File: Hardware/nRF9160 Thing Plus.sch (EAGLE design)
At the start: 89 parts, among them J1 USB Female C, J10 QWIIC_RIGHT_ANGLE, J2 CON-HEADER-1X12-MALE-PIN, J3 CON-HEADER-1X16-MALE-PIN, J4 CON-1909763-1, J6 CON-SIM-104224-0820, J7 CON-1909763-1, J8 CON-FTSH-105-XX-X-DV, Q1 MOSFET-P-SC89, Q2 MOSFET-DUAL-COMP-SOT563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

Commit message: Updated BOM
replaced SW1 and SW2 to new taller momentary switch
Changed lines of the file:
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@@
 <part name="GND11" library="supply1" library_urn="urn:adsk.eagle:library:371" deviceset="GND" device=""/>
 <part name="GND12" library="supply1" library_urn="urn:adsk.eagle:library:371" deviceset="GND" device=""/>
-<part name="SW1" library="SparkFun-Switches" deviceset="MOMENTARY-SWITCH-SPST" device="-SMD-4.6X2.8MM"/>
-<part name="SW2" library="SparkFun-Switches" deviceset="MOMENTARY-SWITCH-SPST" device="-SMD-4.6X2.8MM"/>
+<part name="SW1" library="SparkFun-Switches" deviceset="MOMENTARY-SWITCH-SPST" device="-SMD-4.6X2.8MM" value=""/>
+<part name="SW2" library="SparkFun-Switches" deviceset="MOMENTARY-SWITCH-SPST" device="-SMD-4.6X2.8MM" value=""/>
 <part name="GND13" library="supply1" library_urn="urn:adsk.eagle:library:371" deviceset="GND" device=""/>
 <part name="U6" library="nRF9160-IC" deviceset="FLASH" device="-WSON" package3d_urn="urn:adsk.eagle:package:19416409/2" override_package3d_urn="urn:adsk.eagle:package:19415944/2" override_package_urn="urn:adsk.eagle:footprint:19415945/1" override_locally_modified="yes" technology="-W25Q32JVZPIQ" value="FLASH-WSON"/>

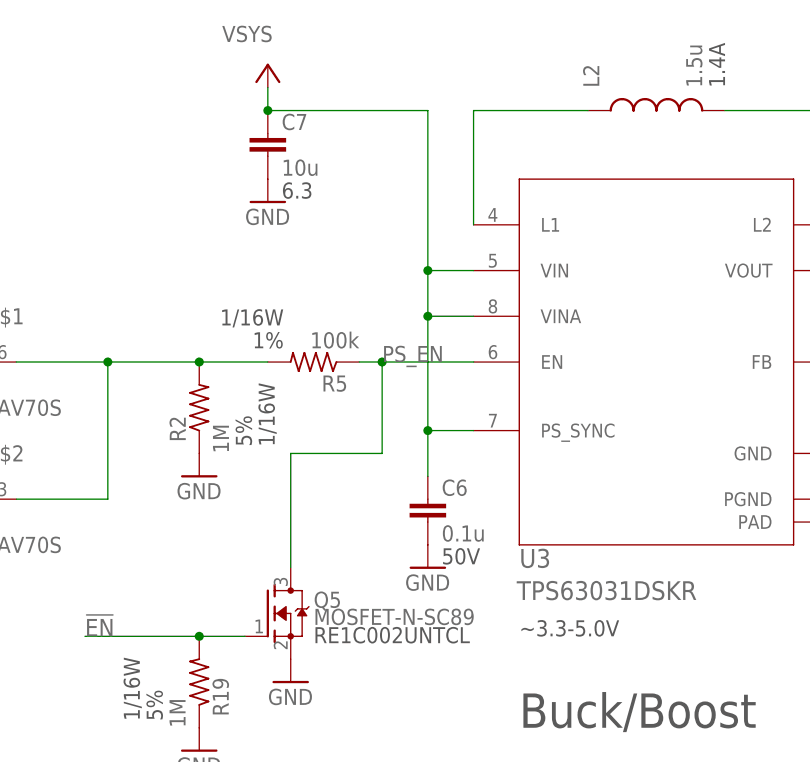
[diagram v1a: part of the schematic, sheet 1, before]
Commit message: Making adjustments to power supply
Changed:
* Pin 7 of U3 grounded.
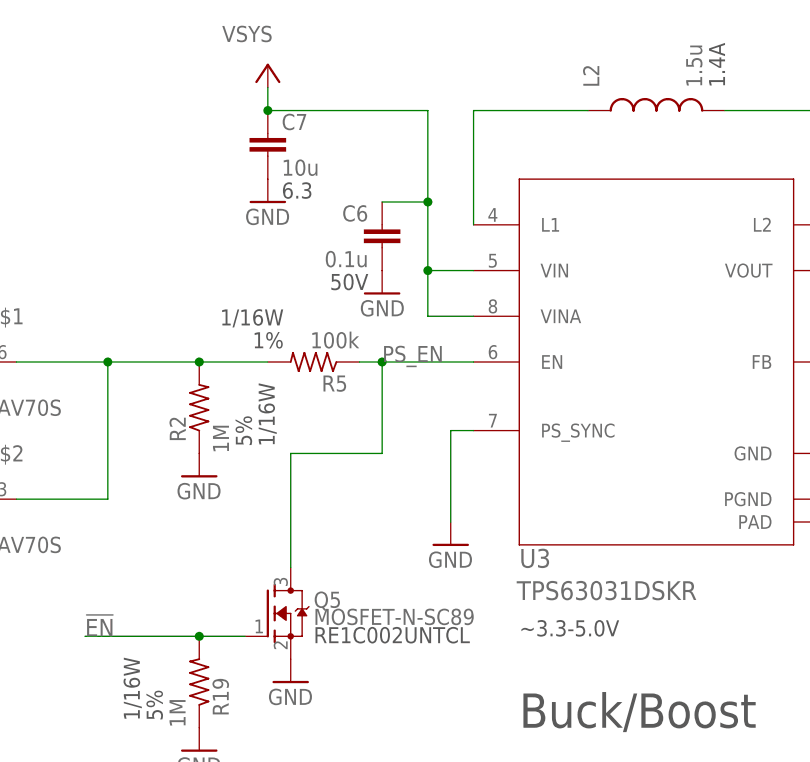
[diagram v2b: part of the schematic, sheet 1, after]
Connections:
- net GND: now also U3.PS_SYNC
- net VSYS: no longer U3.PS_SYNC
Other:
- moved on the sheet: C6
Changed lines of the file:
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@@
 <drawing>
 <settings>
-<setting alwaysvectorfont="yes"/>
+<setting alwaysvectorfont="no"/>
 <setting keepoldvectorfont="yes"/>
 <setting verticaltext="up"/>
@@
 <part name="TP6" library="wolff-den" library_urn="urn:adsk.eagle:library:6370453" deviceset="TP" device="-1SIDE-1P0" package3d_urn="urn:adsk.eagle:package:24898411/1"/>
 <part name="U$24" library="wolff-den" library_urn="urn:adsk.eagle:library:6370453" deviceset="FIDUCIAL" device="-1MM" package3d_urn="urn:adsk.eagle:package:19416411/3" override_package3d_urn="urn:adsk.eagle:package:19416091/2" override_package_urn="urn:adsk.eagle:footprint:19416092/1" override_locally_modified="yes"/>
+<part name="GND2" library="supply1" library_urn="urn:adsk.eagle:library:371" deviceset="GND" device=""/>
 </parts>
 <sheets>
@@
 <attribute name="VALUE" x="91.44" y="228.6" size="1.778" layer="96"/>
 </instance>
-<instance part="C6" gate="A" x="111.76" y="198.12" smashed="yes">
-<attribute name="NAME" x="113.284" y="198.501" size="1.778" layer="95"/>
-<attribute name="VALUE" x="113.284" y="193.421" size="1.778" layer="96"/>
-<attribute name="VOLTHIGH" x="113.284" y="190.881" size="1.778" layer="97"/>
-</instance>
-<instance part="GND21" gate="1" x="111.76" y="190.5" smashed="yes">
-<attribute name="VALUE" x="109.22" y="187.96" size="1.778" layer="96"/>
+<instance part="C6" gate="A" x="106.68" y="228.6" smashed="yes" rot="MR0">
+<attribute name="NAME" x="105.156" y="228.981" size="1.778" layer="95" rot="MR0"/>
+<attribute name="VALUE" x="105.156" y="223.901" size="1.778" layer="96" rot="MR0"/>
+<attribute name="VOLTHIGH" x="105.156" y="221.361" size="1.778" layer="97" rot="MR0"/>
+</instance>
+<instance part="GND21" gate="1" x="106.68" y="220.98" smashed="yes" rot="MR0">
+<attribute name="VALUE" x="109.22" y="218.44" size="1.778" layer="96" rot="MR0"/>
 </instance>
 <instance part="+3V2" gate="G$1" x="182.88" y="233.68" smashed="yes">
@@
 </instance>
 <instance part="U$24" gate="G$1" x="416.56" y="48.26" smashed="yes"/>
+<instance part="GND2" gate="1" x="114.3" y="193.04" smashed="yes">
+<attribute name="VALUE" x="111.76" y="190.5" size="1.778" layer="96"/>
+</instance>
 </instances>
 <busses>
@@
 <pinref part="R20" gate="R1" pin="1"/>
 <pinref part="GND44" gate="1" pin="GND"/>
+</segment>
+<segment>
+<pinref part="GND2" gate="1" pin="GND"/>
+<wire x1="114.3" y1="195.58" x2="114.3" y2="205.74" width="0.1524" layer="91"/>
+<pinref part="U3" gate="A" pin="PS_SYNC"/>
+<wire x1="114.3" y1="205.74" x2="116.84" y2="205.74" width="0.1524" layer="91"/>
 </segment>
 </net>
@@
 <junction x="93.98" y="241.3"/>
 <wire x1="116.84" y1="218.44" x2="111.76" y2="218.44" width="0.1524" layer="91"/>
-<wire x1="111.76" y1="218.44" x2="111.76" y2="205.74" width="0.1524" layer="91"/>
-<wire x1="111.76" y1="205.74" x2="116.84" y2="205.74" width="0.1524" layer="91"/>
 <pinref part="C6" gate="A" pin="1"/>
-<wire x1="111.76" y1="205.74" x2="111.76" y2="200.66" width="0.1524" layer="91"/>
-<junction x="111.76" y="205.74"/>
 <wire x1="111.76" y1="218.44" x2="111.76" y2="223.52" width="0.1524" layer="91"/>
-<junction x="111.76" y="218.44"/>
 <junction x="111.76" y="223.52"/>
 <wire x1="93.98" y1="241.3" x2="111.76" y2="241.3" width="0.1524" layer="91"/>
-<wire x1="111.76" y1="241.3" x2="111.76" y2="223.52" width="0.1524" layer="91"/>
+<wire x1="111.76" y1="241.3" x2="111.76" y2="231.14" width="0.1524" layer="91"/>
 <pinref part="U3" gate="A" pin="VIN"/>
-<pinref part="U3" gate="A" pin="PS_SYNC"/>
 <pinref part="U3" gate="A" pin="VINA"/>
-</segment>
-<segment>
+<wire x1="111.76" y1="231.14" x2="111.76" y2="223.52" width="0.1524" layer="91"/>
+<wire x1="106.68" y1="231.14" x2="111.76" y2="231.14" width="0.1524" layer="91"/>
+<junction x="111.76" y="231.14"/>
+</segment>
+<segment>
